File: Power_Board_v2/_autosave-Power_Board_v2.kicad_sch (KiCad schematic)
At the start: 33 parts, among them J1 Conn_02x16_Odd_Even, Q1 MMBT5551L, U2 HUSB237-AA001-DN06R, U3 BQ24074RGT, U4 INA219AxDCN SOT-23

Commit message: Updated footprints and battery label
I HATE THE IMPERIAL SYSTEM
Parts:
- C4, C5, C6, C7, C8: footprint Capacitor_SMD:C_0201_0603Metric_Pad0.64x0.40mm_HandSolder -> Capacitor_SMD:C_0603_1608Metric_Pad1.08x0.95mm_HandSolder
- D1, D2: footprint LED_SMD:LED_0201_0603Metric_Pad0.64x0.40mm_HandSolder -> LED_SMD:LED_0603_1608Metric_Pad1.05x0.95mm_HandSolder
- R10, R11, R12, R13, R15, R16, R18, R2, R3, R7, R9: footprint Resistor_SMD:R_0201_0603Metric_Pad0.64x0.40mm_HandSolder -> Resistor_SMD:R_0603_1608Metric_Pad0.98x0.95mm_HandSolder
- R14, R17: footprint Resistor_SMD:R_0805_2012Metric_Pad1.20x1.40mm_HandSolder -> Resistor_SMD:R_1206_3216Metric_Pad1.30x1.75mm_HandSolder
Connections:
- net BATT renamed Battery
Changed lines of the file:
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@@
 		)
 	)
-	(label "BATT"
+	(label "Battery"
 		(at 196.85 25.4 0)
 		(effects
@@
 		)
 	)
-	(label "BATT"
+	(label "Battery"
 		(at 35.56 33.02 0)
 		(effects
@@
 		)
 	)
-	(label "BATT"
+	(label "Battery"
 		(at 375.92 41.91 0)
 		(effects
@@
 		)
 	)
-	(label "BATT"
+	(label "Battery"
 		(at 35.56 68.58 0)
 		(effects
@@
 			)
 		)
-		(property "Footprint" "Resistor_SMD:R_0201_0603Metric_Pad0.64x0.40mm_HandSolder"
+		(property "Footprint" "Resistor_SMD:R_0603_1608Metric_Pad0.98x0.95mm_HandSolder"
 			(at 195.58 60.96 0)
 			(effects
@@
 			)
 		)
-		(property "Footprint" "Resistor_SMD:R_0201_0603Metric_Pad0.64x0.40mm_HandSolder"
+		(property "Footprint" "Resistor_SMD:R_0603_1608Metric_Pad0.98x0.95mm_HandSolder"
 			(at 71.12 40.64 0)
 			(effects
@@
 			)
 		)
-		(property "Footprint" "Resistor_SMD:R_0201_0603Metric_Pad0.64x0.40mm_HandSolder"
+		(property "Footprint" "Resistor_SMD:R_0603_1608Metric_Pad0.98x0.95mm_HandSolder"
 			(at 148.59 53.34 0)
 			(effects
@@
 			)
 		)
-		(property "Footprint" "Capacitor_SMD:C_0201_0603Metric_Pad0.64x0.40mm_HandSolder"
+		(property "Footprint" "Capacitor_SMD:C_0603_1608Metric_Pad1.08x0.95mm_HandSolder"
 			(at 190.5 58.42 0)
 			(effects
@@
 			)
 		)
-		(property "Footprint" "Capacitor_SMD:C_0201_0603Metric_Pad0.64x0.40mm_HandSolder"
+		(property "Footprint" "Capacitor_SMD:C_0603_1608Metric_Pad1.08x0.95mm_HandSolder"
 			(at 148.59 27.94 0)
 			(effects
@@
 			)
 		)
-		(property "Footprint" "Resistor_SMD:R_0201_0603Metric_Pad0.64x0.40mm_HandSolder"
+		(property "Footprint" "Resistor_SMD:R_0603_1608Metric_Pad0.98x0.95mm_HandSolder"
 			(at 148.59 48.26 0)
 			(effects
@@
 			)
 		)
-		(property "Footprint" "Resistor_SMD:R_0201_0603Metric_Pad0.64x0.40mm_HandSolder"
+		(property "Footprint" "Resistor_SMD:R_0603_1608Metric_Pad0.98x0.95mm_HandSolder"
 			(at 71.12 64.77 0)
 			(effects
@@
 			)
 		)
-		(property "Footprint" "Resistor_SMD:R_0201_0603Metric_Pad0.64x0.40mm_HandSolder"
+		(property "Footprint" "Resistor_SMD:R_0603_1608Metric_Pad0.98x0.95mm_HandSolder"
 			(at 157.48 88.9 0)
 			(effects
@@
 			)
 		)
-		(property "Footprint" "LED_SMD:LED_0201_0603Metric_Pad0.64x0.40mm_HandSolder"
+		(property "Footprint" "LED_SMD:LED_0603_1608Metric_Pad1.05x0.95mm_HandSolder"
 			(at 201.93 43.18 90)
 			(effects
@@
 			)
 		)
-		(property "Footprint" "Resistor_SMD:R_0201_0603Metric_Pad0.64x0.40mm_HandSolder"
+		(property "Footprint" "Resistor_SMD:R_0603_1608Metric_Pad0.98x0.95mm_HandSolder"
 			(at 201.93 35.56 0)
 			(effects
@@
 			)
 		)
-		(property "Footprint" "Capacitor_SMD:C_0201_0603Metric_Pad0.64x0.40mm_HandSolder"
+		(property "Footprint" "Capacitor_SMD:C_0603_1608Metric_Pad1.08x0.95mm_HandSolder"
 			(at 78.74 54.61 0)
 			(effects
@@
 			)
 		)
-		(property "Footprint" "Resistor_SMD:R_0201_0603Metric_Pad0.64x0.40mm_HandSolder"
+		(property "Footprint" "Resistor_SMD:R_0603_1608Metric_Pad0.98x0.95mm_HandSolder"
 			(at 143.51 62.23 0)
 			(effects
@@
 			)
 		)
-		(property "Footprint" "Capacitor_SMD:C_0201_0603Metric_Pad0.64x0.40mm_HandSolder"
+		(property "Footprint" "Capacitor_SMD:C_0603_1608Metric_Pad1.08x0.95mm_HandSolder"
 			(at 218.44 39.37 0)
 			(effects
@@
 			)
 		)
-		(property "Footprint" "Capacitor_SMD:C_0201_0603Metric_Pad0.64x0.40mm_HandSolder"
+		(property "Footprint" "Capacitor_SMD:C_0603_1608Metric_Pad1.08x0.95mm_HandSolder"
 			(at 63.5 152.4 0)
 			(effects
@@
 			)
 		)
-		(property "Footprint" "Resistor_SMD:R_0201_0603Metric_Pad0.64x0.40mm_HandSolder"
+		(property "Footprint" "Resistor_SMD:R_0603_1608Metric_Pad0.98x0.95mm_HandSolder"
 			(at 210.82 35.56 0)
 			(effects
@@
 			)
 		)
-		(property "Footprint" "Resistor_SMD:R_0201_0603Metric_Pad0.64x0.40mm_HandSolder"
+		(property "Footprint" "Resistor_SMD:R_0603_1608Metric_Pad0.98x0.95mm_HandSolder"
 			(at 139.7 67.31 0)
 			(effects
@@
 			)
 		)
-		(property "Footprint" "LED_SMD:LED_0201_0603Metric_Pad0.64x0.40mm_HandSolder"
+		(property "Footprint" "LED_SMD:LED_0603_1608Metric_Pad1.05x0.95mm_HandSolder"
 			(at 210.82 43.18 90)
 			(effects
@@
 			)
 		)
-		(property "Footprint" "Resistor_SMD:R_0805_2012Metric_Pad1.20x1.40mm_HandSolder"
+		(property "Footprint" "Resistor_SMD:R_1206_3216Metric_Pad1.30x1.75mm_HandSolder"
 			(at 33.02 52.07 0)
 			(effects
@@
 			)
 		)
-		(property "Footprint" "Resistor_SMD:R_0805_2012Metric_Pad1.20x1.40mm_HandSolder"
+		(property "Footprint" "Resistor_SMD:R_1206_3216Metric_Pad1.30x1.75mm_HandSolder"
 			(at 39.37 52.07 0)
 			(effects
@@
 			)
 		)
-		(property "Footprint" "Resistor_SMD:R_0201_0603Metric_Pad0.64x0.40mm_HandSolder"
+		(property "Footprint" "Resistor_SMD:R_0603_1608Metric_Pad0.98x0.95mm_HandSolder"
 			(at 71.12 152.4 0)
 			(effects

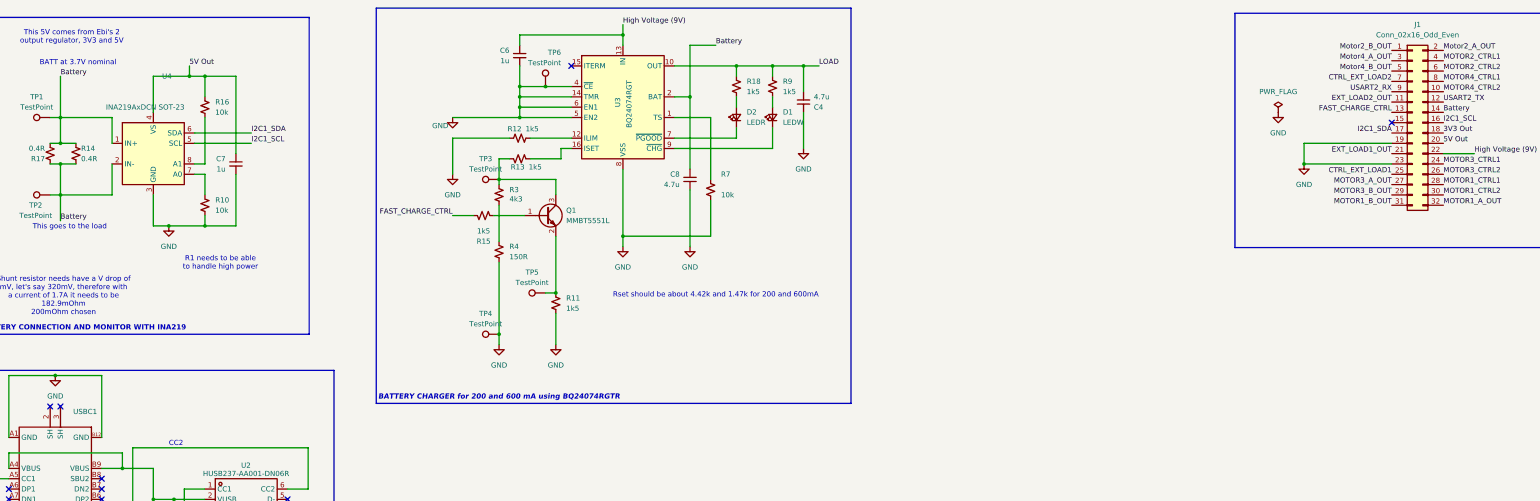
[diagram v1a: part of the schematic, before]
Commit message: Updated parts' details to get correct BOM
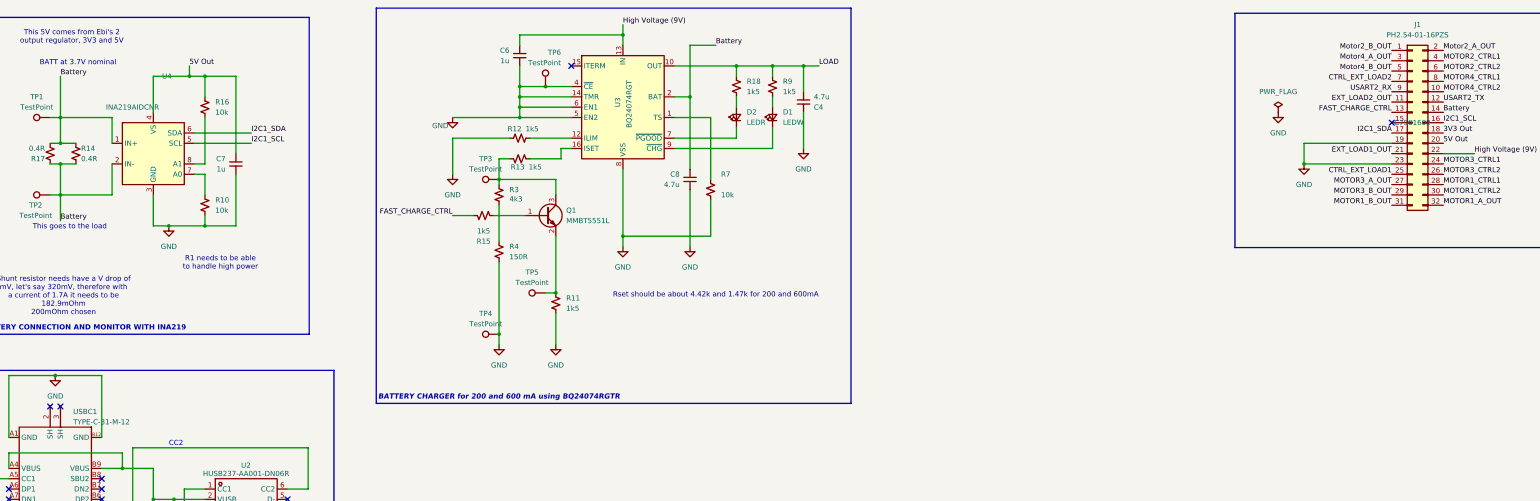
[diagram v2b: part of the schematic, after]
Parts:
- J1: value Conn_02x16_Odd_Even -> PH2.54-01-16PZS; LCSC (none) -> C7501602
- U4: value INA219AxDCN SOT-23 -> INA219AIDCNR
- USBC1: value ~ -> TYPE-C-31-M-12
